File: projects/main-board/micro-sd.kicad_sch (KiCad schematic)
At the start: 4 parts, among them U13 DM3AT-SF-PEJM5

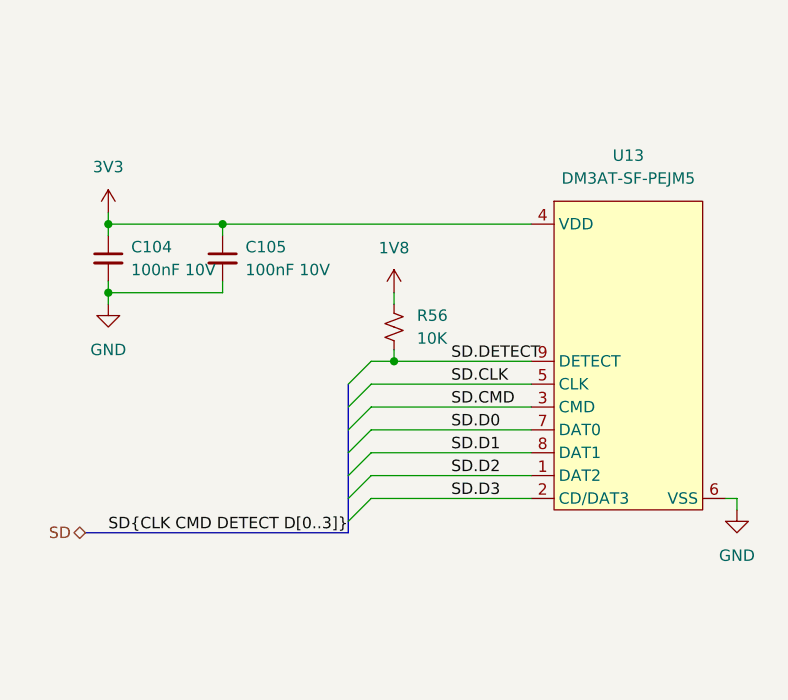
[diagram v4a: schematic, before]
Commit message: Add footprints
- Inductors
- Switches
- Buttons
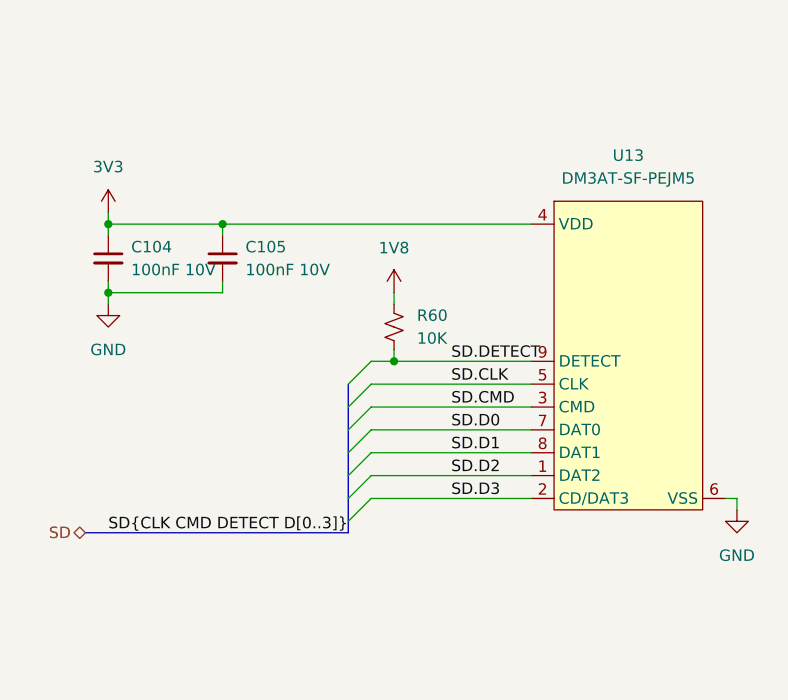
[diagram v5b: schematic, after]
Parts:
- renumbered R56 to R60
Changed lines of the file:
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@@
 		(dnp no)
 		(fields_autoplaced yes)
-		(property "Reference" "#PWR0147"
+		(property "Reference" "#PWR0148"
 			(at 111.76 85.09 0)
 			(effects
@@
 			(project ""
 				(path "/c621b5fd-2ef7-4a67-960d-0ffc72b1245a/78e3df9a-9d0e-4599-9dc1-8d07bc071d30"
-					(reference "#PWR0147")
+					(reference "#PWR0148")
 					(unit 1)
 				)
@@
 		(dnp no)
 		(fields_autoplaced yes)
-		(property "Reference" "#PWR0150"
+		(property "Reference" "#PWR0151"
 			(at 181.61 120.65 0)
 			(effects
@@
 			(project ""
 				(path "/c621b5fd-2ef7-4a67-960d-0ffc72b1245a/78e3df9a-9d0e-4599-9dc1-8d07bc071d30"
-					(reference "#PWR0150")
+					(reference "#PWR0151")
 					(unit 1)
 				)
@@
 		(dnp no)
 		(fields_autoplaced yes)
-		(property "Reference" "R56"
+		(property "Reference" "R60"
 			(at 146.05 92.7099 0)
 			(effects
@@
 			(project "main-board"
 				(path "/c621b5fd-2ef7-4a67-960d-0ffc72b1245a/78e3df9a-9d0e-4599-9dc1-8d07bc071d30"
-					(reference "R56")
+					(reference "R60")
 					(unit 1)
 				)
@@
 		(dnp no)
 		(fields_autoplaced yes)
-		(property "Reference" "#PWR0149"
+		(property "Reference" "#PWR0150"
 			(at 143.51 93.98 0)
 			(effects
@@
 			(project "main-board"
 				(path "/c621b5fd-2ef7-4a67-960d-0ffc72b1245a/78e3df9a-9d0e-4599-9dc1-8d07bc071d30"
-					(reference "#PWR0149")
+					(reference "#PWR0150")
 					(unit 1)
 				)
@@
 		(dnp no)
 		(fields_autoplaced yes)
-		(property "Reference" "#PWR0148"
+		(property "Reference" "#PWR0149"
 			(at 111.76 97.79 0)
 			(effects
@@
 			(project "main-board"
 				(path "/c621b5fd-2ef7-4a67-960d-0ffc72b1245a/78e3df9a-9d0e-4599-9dc1-8d07bc071d30"
-					(reference "#PWR0148")
-					(unit 1)
-				)
+					(reference "#PWR0149")
+					(unit 1)
+				)

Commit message: Fix footprint DRC errors.
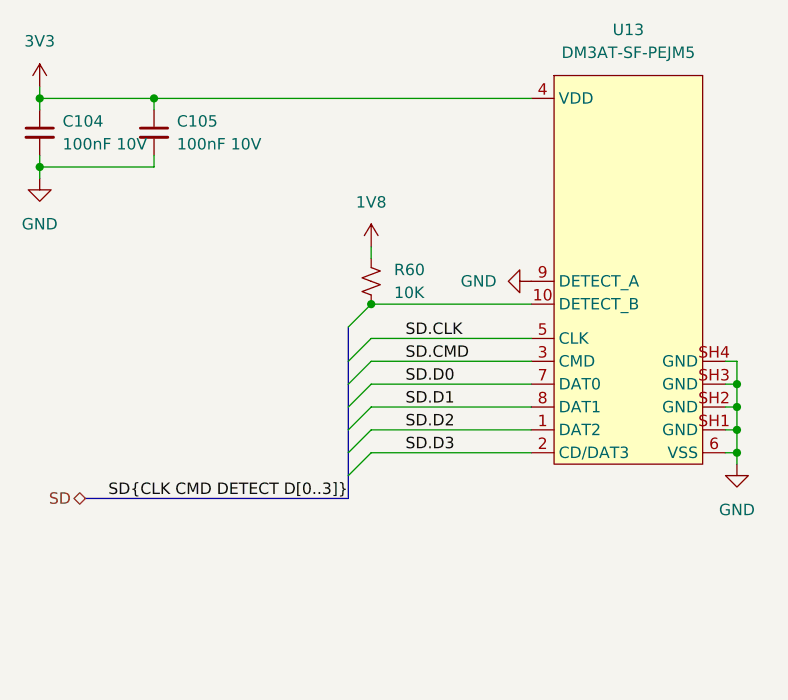
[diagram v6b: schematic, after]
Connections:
- net GND: now also U13.9 (DETECT_A), U13.SH1 (GND), U13.SH2 (GND), U13.SH3 (GND), U13.SH4 (GND)
- net SD.DETECT: no longer names the net of R60.2
- net SD.DETECT: now also U13.10 (DETECT_B); no longer U13.9 (DETECT)
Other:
- moved on the sheet: C104, C105, R60

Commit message: WIP splitting main board into 3
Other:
- moved on the sheet: C104, C105, R60, U13
